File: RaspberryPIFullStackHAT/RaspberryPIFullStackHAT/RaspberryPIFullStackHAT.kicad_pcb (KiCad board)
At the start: 2 copper layers, 28.2 x 17.9 mm, 9 parts, among them J1 Raspberry_Pi_2_3, SW1 SW_DPST, U1 DHT22

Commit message: no message
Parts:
- U1: footprint Connector_PinHeader_2.54mm:PinHeader_1x03_P2.54mm_Vertical -> Connector_PinHeader_2.54mm:PinHeader_1x04_P2.54mm_Vertical
- moved D1 12.7 mm to (129.4, 85.2)
- moved R3 12.3 mm to (125.3, 86.7)
- moved D2 9.40 mm to (108.0, 86.2), turned to 90 degrees
- moved R2 8.36 mm to (112.6, 86.2), turned to 270 degrees
- moved R1 3.01 mm to (102.6, 85.9)
- moved R4 2.93 mm to (110.4, 86.2), turned to 90 degrees
- moved U1 0.44 mm to (117.3, 92.8)
- moved J1 0.13 mm to (99.8, 82.7)
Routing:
- net +3V3: track 0.80 -> 32.8 mm
- net /button_input: track 0.00 -> 20.1 mm
- net GND: track 0.00 -> 11.8 mm, vias 0 -> 2
- net /DHT22_input: track 0.00 -> 3.04 mm
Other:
- outline, holes or cut-outs redrawn

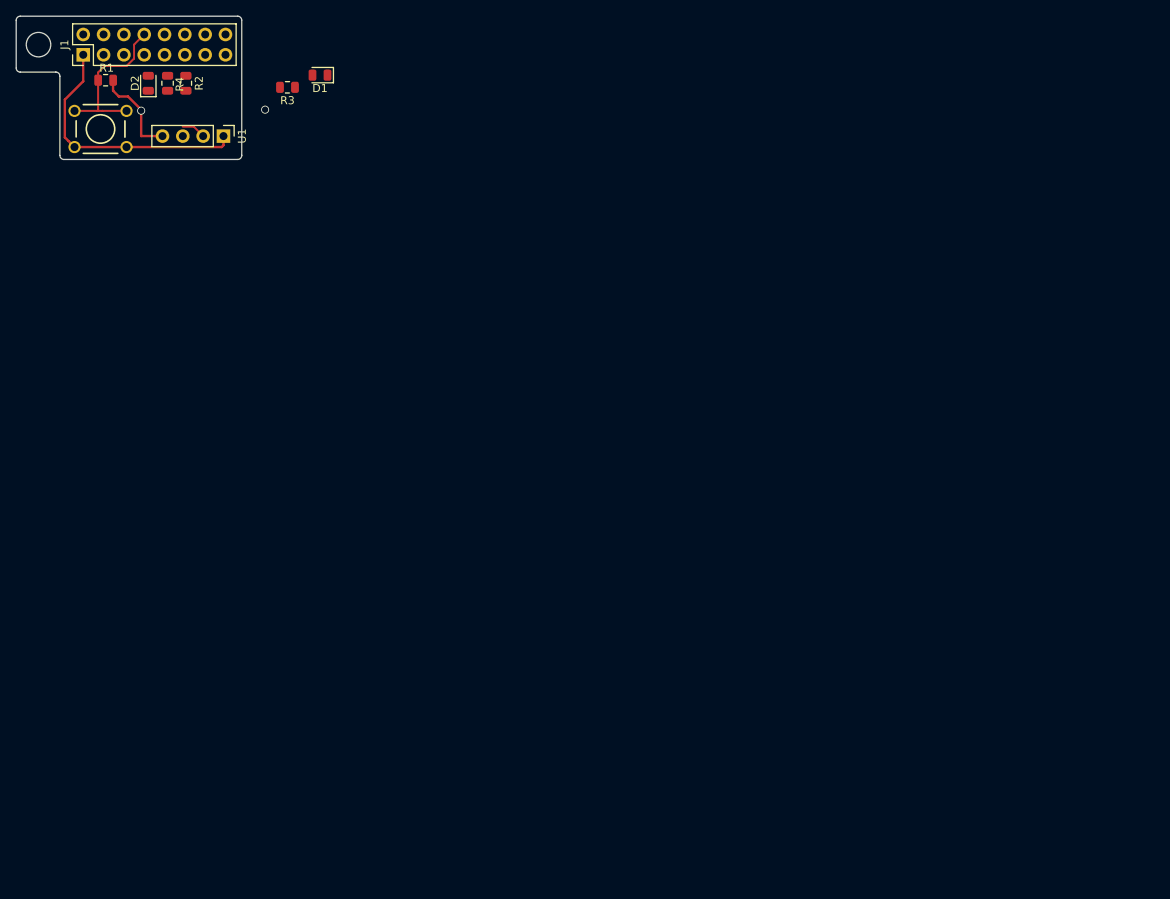
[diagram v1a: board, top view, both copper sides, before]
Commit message: main readme updated, LCD RPI3 HAT updated
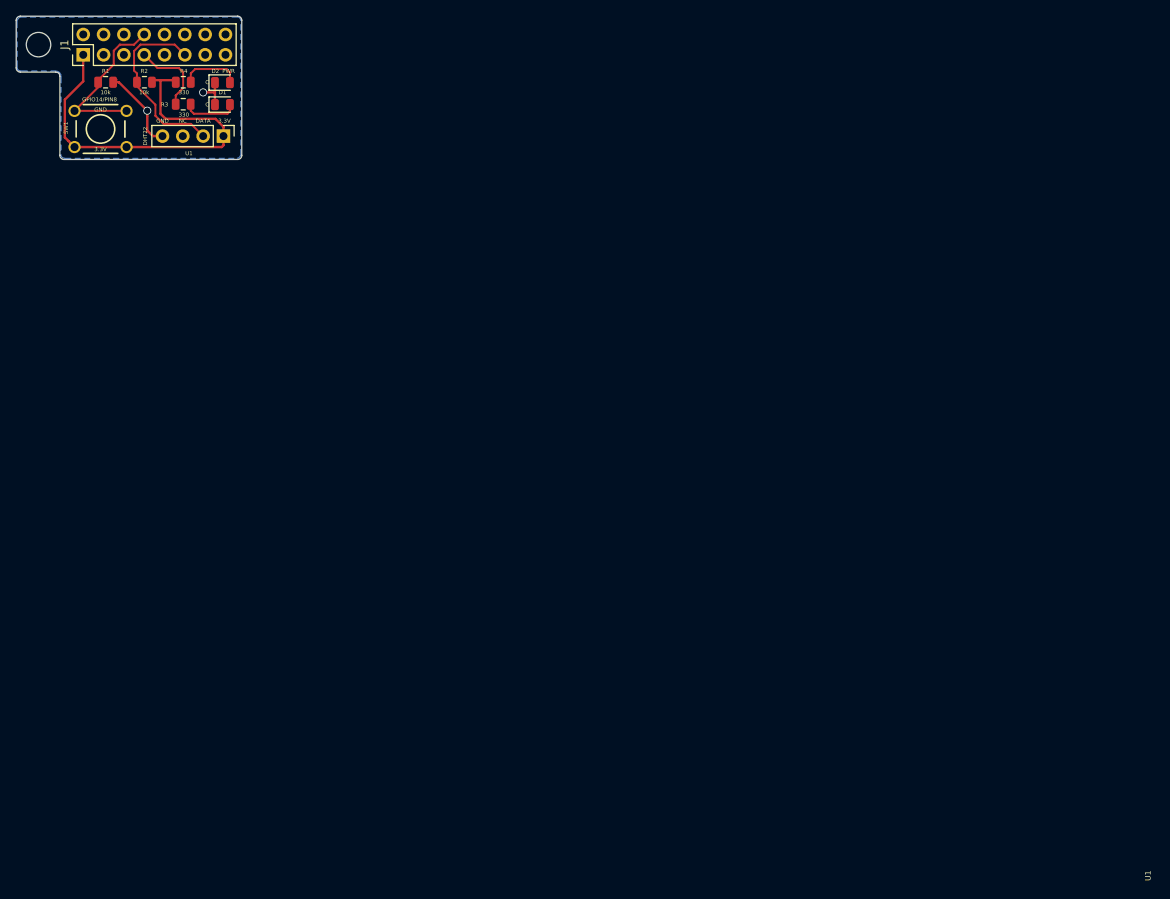
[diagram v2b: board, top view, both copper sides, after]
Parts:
- added ?: , , F.Cu at (116.3, 98.2)
- added REF**: KiCad-Logo_5mm_SilkScreen, Symbol:KiCad-Logo_5mm_SilkScreen, B.Cu at (105.9, 89.9)
- R1, R2: value R -> 10k
- R3, R4: value R -> 330
- moved R3 13.2 mm to (112.3, 88.9)
- moved D1 12.7 mm to (117.2, 88.9), turned to 0 degrees
- moved D2 9.27 mm to (117.2, 86.2), turned to 0 degrees
- moved R2 5.18 mm to (107.5, 86.1), turned to 180 degrees
- moved R4 1.97 mm to (112.3, 86.1), turned to 180 degrees
- moved R1 0.25 mm to (102.6, 86.1)
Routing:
- net /DHT22_input: track 3.04 -> 23.4 mm
- net +3V3: track 32.8 -> 49.7 mm
- net /led_output: track 0.00 -> 10.1 mm
- net Net-(D2-Pad2): track 0.00 -> 7.07 mm
- net Net-(D1-Pad2): track 0.00 -> 6.83 mm
- net GND: track 11.8 -> 15.4 mm
- net /button_input: track 20.1 -> 20.8 mm
- added copper zone on B.Cu, net GND
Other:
- board text added: "3.3V"
- board text added: "C"
- board text added: "DATA"
- board text added: "GND"
- board text added: "GPIO04 LED GPIO14 Button"
- board text added: "GPIO14/PIN8"
- board text added: "NC"
- board text added: "PWR"
- board text added: "Raspberry Pi Full Stack Version 1"
